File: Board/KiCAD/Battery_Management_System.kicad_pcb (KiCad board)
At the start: 4 copper layers, 104 parts, among them J1 Conn_01x06_Socket, J2 Conn_ARM_SWD_TagConnect_TC2030, J4 Conn_01x03, J5 Conn_01x03, J7 Conn_01x05, J8 Conn_01x02, J9 Conn_01x02, Q1 AON7408, Q10 AON7407, Q2 AON7408, Q23 2N7002, Q24 2N7002, Q25 2N7002, Q26 2N7002, Q3 AON7408, Q4 AON7408, Q5 BSS83P, Q6 BSS83P, Q7 BSS83P, Q8 BSS83P, SW2 SW_Push, U1 BQ25730RSNR, U3 LTC2943CDD_PBF, U4 INA260, U5 LMR50410, U6 INA260, U7 INA260, U8 INA260, U9 STM32F103C8T6, Y4 CM8V-T1A-32.768KHZ-12.5PF-20P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, Y5 8MHz

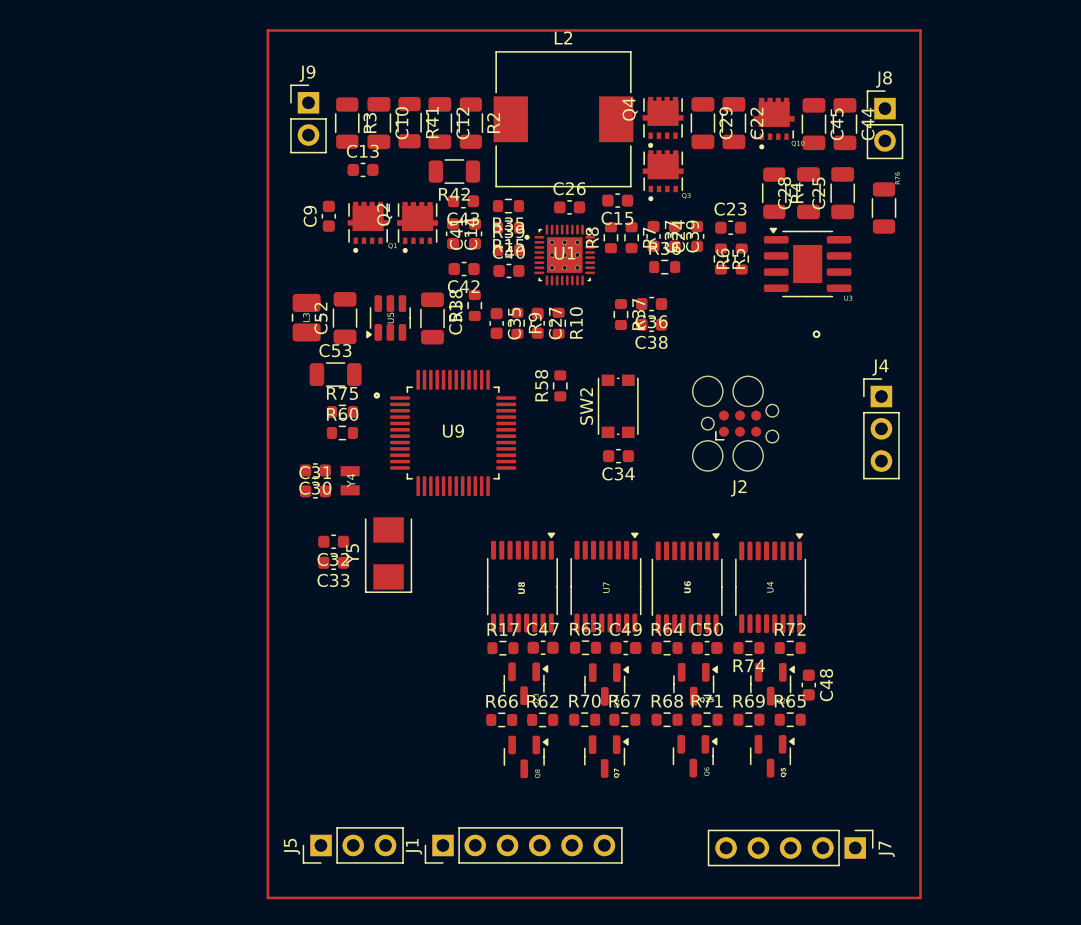
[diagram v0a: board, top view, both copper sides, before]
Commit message: Schematic: - Fixed FDI plug - Added thermistor connectors - Added a bunch of NCs using KiCAD NC tool - Added filter cap back into battery current shunt - Added bypass cap to LTC - Removed Cell 4 INA260 because the LTC does current, voltage of that top cell! Board Layout: - Chewed out team for not reading the BQ's datasheet, specifically Section 11 - Relayed out power stream using Section 11 as a refernce - Changed some footprints, mostly reducing size to 0603 - Positioned things optimally given what I thought made sense (dangerous, I know) - Fixed ground planes Other: - Removed PRL and CACHE files from the repo.
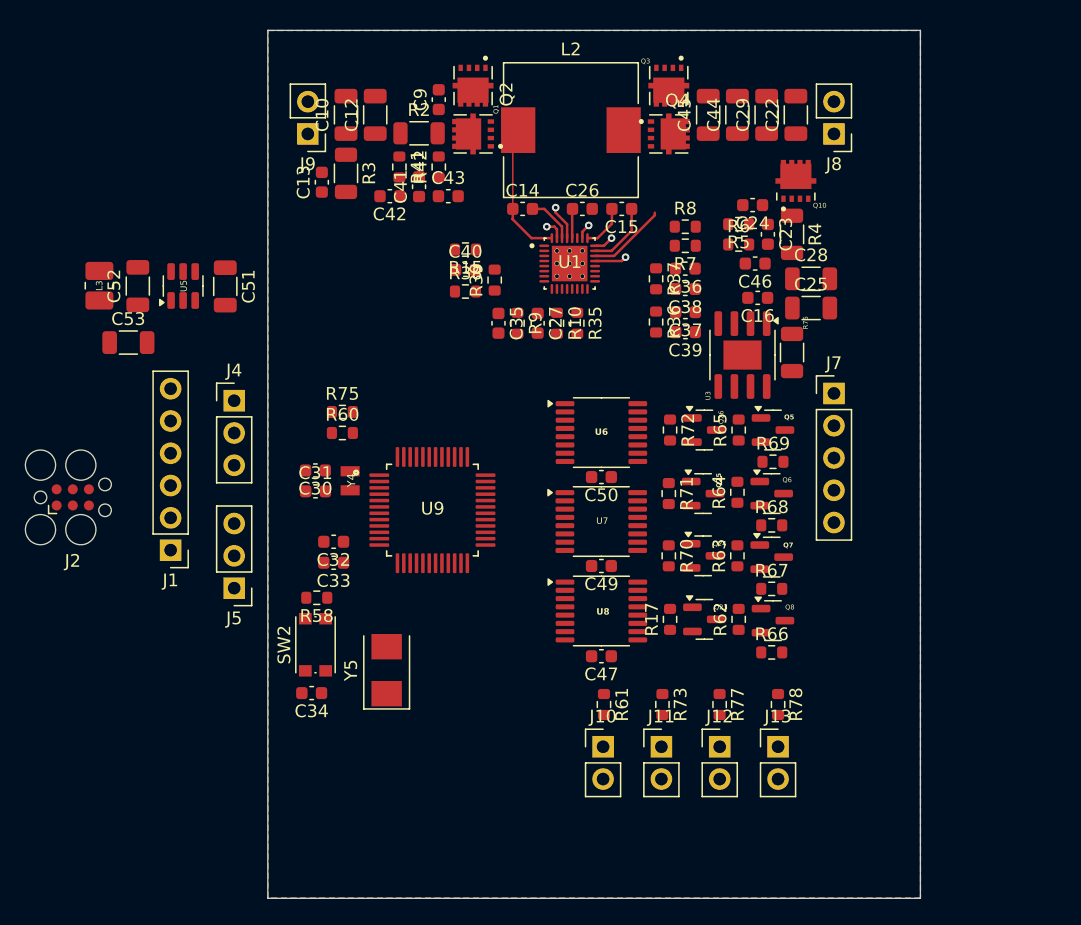
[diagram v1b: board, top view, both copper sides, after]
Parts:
- removed C48: 100n, Capacitor_SMD:C_0603_1608Metric
- removed R74: R_Small, Resistor_SMD:R_0603_1608Metric
- removed U4: INA260, Package_SO:TSSOP-16_4.4x5mm_P0.65mm
- added C16: 1uF, Capacitor_SMD:C_0603_1608Metric, F.Cu at (241.7, 67.7)
- added C46: 0.1uF, Capacitor_SMD:C_0603_1608Metric, F.Cu at (241.5, 65.0)
- added J10: Conn_01x02, Connector_PinHeader_2.54mm:PinHeader_1x02_P2.54mm_Vertical, F.Cu at (229.5, 103.0)
- added J11: Conn_01x02, Connector_PinHeader_2.54mm:PinHeader_1x02_P2.54mm_Vertical, F.Cu at (234.1, 103.0)
- added J12: Conn_01x02, Connector_PinHeader_2.54mm:PinHeader_1x02_P2.54mm_Vertical, F.Cu at (238.7, 103.0)
- added J13: Conn_01x02, Connector_PinHeader_2.54mm:PinHeader_1x02_P2.54mm_Vertical, F.Cu at (243.3, 103.0)
- added R61: 10k, Resistor_SMD:R_0603_1608Metric, F.Cu at (229.6, 99.7)
- added R73: 10k, Resistor_SMD:R_0603_1608Metric, F.Cu at (234.2, 99.7)
- added R77: 10k, Resistor_SMD:R_0603_1608Metric, F.Cu at (238.7, 99.7)
- added R78: 10k, Resistor_SMD:R_0603_1608Metric, F.Cu at (243.3, 99.7)
- R41, R42: footprint Resistor_SMD:R_1206_3216Metric -> Resistor_SMD:R_0603_1608Metric
- U3: value LTC2943CDD_PBF -> LTC2943CDD#PBF
- moved J2 52.8 mm to (187.8, 83.4)
- moved J4 50.9 mm to (200.5, 75.8)
- moved J7 35.8 mm to (247.7, 75.2), turned to 0 degrees
- moved J1 31.6 mm to (195.5, 87.5), turned to 180 degrees
- moved C34 30.5 mm to (206.6, 98.8)
- moved SW2 30.3 mm to (206.9, 95.0)
- moved Q5 25.7 mm to (242.9, 78.1), turned to 0 degrees
- moved R58 25.4 mm to (207.0, 91.3), turned to 180 degrees
- moved R65 23.2 mm to (240.2, 78.1), turned to 90 degrees
- moved Q8 22.3 mm to (242.9, 93.1), turned to 0 degrees
- moved R66 21.9 mm to (242.8, 95.6)
- moved Q6 21.6 mm to (242.8, 83.1), turned to 0 degrees
- moved J5 21.4 mm to (200.5, 90.5), turned to 180 degrees
- moved Q26 20.7 mm to (237.5, 78.1), turned to 0 degrees
- moved Q7 20.5 mm to (242.8, 88.1), turned to 0 degrees
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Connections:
- J1 pad 1: NC -> unconnected-(J1-Pin_1-Pad1)
- J1 pad 2: /Microcontroller/USART1_RX -> /Microcontroller/USART1_TX
- J1 pad 3: /Microcontroller/USART1_TX -> /Microcontroller/USART1_RX
- J1 pad 4: 3.3V -> unconnected-(J1-Pin_4-Pad4)
- J1 pad 5: NC -> unconnected-(J1-Pin_5-Pad5)
- J7 pad 1: /Cell Interface/Cell 4 -> /Cell Interface/BATT
- Q5 pad 3: /Cell Interface/Cell 4 -> /Cell Interface/BATT
- R65 pad 1: /Cell Interface/Cell 4 -> /Cell Interface/BATT
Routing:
- net Net-(U1-SW1): track 0.00 -> 10.9 mm
- net /Charge Control/Vsys: track 0.00 -> 6.23 mm
- net Net-(U1-SW2): track 0.00 -> 5.25 mm
- net Net-(U1-BTST1): track 0.00 -> 3.80 mm
- net Net-(U1-BTST2): track 0.00 -> 3.57 mm
- net Net-(U1-LODRV1): track 0.00 -> 2.77 mm, vias 0 -> 1
- net Net-(U1-~{BATDRV}): track 0.00 -> 2.52 mm, vias 0 -> 1
- net Net-(U1-REGN): track 0.00 -> 2.36 mm
- net Net-(U1-HIDRV1): track 0.00 -> 1.58 mm, vias 0 -> 1
- net Net-(U1-HIDRV2): track 0.00 -> 1.55 mm, vias 0 -> 1
- net Net-(U1-LODRV2): track 0.00 -> 1.21 mm, vias 0 -> 1
- net GND: vias 1 -> 0
- added copper zone on B.Cu, net GND
- added copper zone on F.Cu, net GND
- added copper zone on In2.Cu, net GND
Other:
- board outline added: 51.3 x 68.3 mm

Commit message: Schematic: - Changed to smaller 4 pin crystal - Added STM32 bypass caps Layout: - Added some example zones around vbus - Initial component placement for STM32 - Did an example Kelvin connection for shunt resistors - Added 3.3V power zone on layer 3 (PWR)
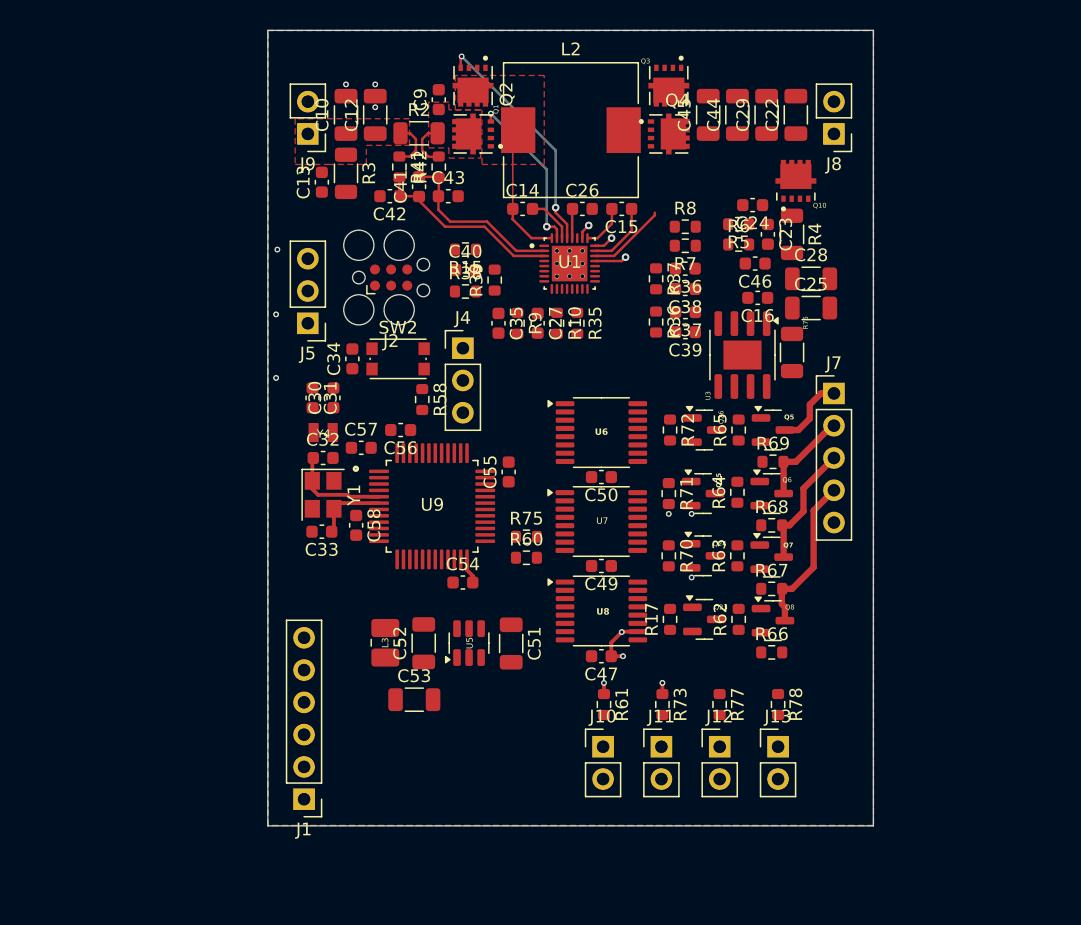
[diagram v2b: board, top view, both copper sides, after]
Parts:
- removed Y5: 8MHz, Crystal:Crystal_SMD_5032-2Pin_5.0x3.2mm
- added C54: 100n, Capacitor_SMD:C_0603_1608Metric, F.Cu at (218.5, 90.1)
- added C55: 100n, Capacitor_SMD:C_0603_1608Metric, F.Cu at (222.1, 81.4)
- added C56: 100n, Capacitor_SMD:C_0603_1608Metric, F.Cu at (213.6, 78.1)
- added C57: 100n, Capacitor_SMD:C_0603_1608Metric, F.Cu at (210.5, 79.5)
- added C58: 100n, Capacitor_SMD:C_0603_1608Metric, F.Cu at (210.1, 85.6)
- added Y1: Crystal_GND24_Small, Crystal:Crystal_SMD_TXC_7M-4Pin_3.2x2.5mm, F.Cu at (207.5, 83.2)
- moved C51 36.0 mm to (222.3, 94.9)
- moved C53 36.0 mm to (214.7, 99.3)
- moved C52 36.0 mm to (215.4, 94.9)
- moved L3 36.0 mm to (212.4, 94.8)
- moved U5 36.0 mm to (219.0, 94.9)
- moved J2 30.4 mm to (212.8, 66.1)
- moved C34 26.5 mm to (209.8, 72.5), turned to 90 degrees
- moved SW2 23.4 mm to (213.4, 72.5), turned to 0 degrees
- moved J1 22.2 mm to (206.0, 107.2)
- moved J5 21.6 mm to (206.3, 69.7)
- moved J4 18.5 mm to (218.5, 71.7)
- moved R58 17.7 mm to (215.3, 75.7), turned to -90 degrees
- moved R75 17.5 mm to (223.5, 86.5)
- moved R60 17.5 mm to (223.5, 88.2)
- moved C31 7.35 mm to (206.7, 75.6), turned to -90 degrees
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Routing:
- net Net-(U1-LODRV1): track 2.77 -> 18.7 mm, vias 1 -> 2
- net Net-(U1-ACP): track 0.00 -> 15.0 mm
- net Net-(U1-ACN): track 0.00 -> 13.8 mm
- net /Cell Interface/Cell 1: track 0.00 -> 12.5 mm
- net Net-(U1-HIDRV1): track 1.58 -> 12.9 mm, vias 1 -> 2
- net /Cell Interface/Cell 2: track 0.00 -> 9.87 mm
- net 3.3V: track 0.00 -> 8.24 mm, vias 0 -> 4
- net Net-(U9-PD0_OSC_IN): track 0.00 -> 7.97 mm
- net /Cell Interface/Cell 3: track 0.00 -> 7.66 mm
- net /Cell Interface/BATT: track 0.00 -> 5.70 mm
- net Net-(U9-PD1_OSC_OUT): track 0.00 -> 5.60 mm
- net Net-(C9-Pad1): track 0.00 -> 3.82 mm
- net /Charge Control/VBus: track 0.00 -> 3.80 mm
- net GND: vias 0 -> 9
- added copper zone on F.Cu, net /Charge Control/VBus
- added copper zone on In2.Cu, net 3.3V
- added copper zone on F.Cu, net Net-(C9-Pad1)
- added copper zone on F.Cu, net Net-(U1-SW1)
- removed copper zone on In2.Cu, net /Charge Control/VBus
- removed copper zone on In2.Cu, net /Charge Control/Vsys
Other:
- board size 51.3 x 68.3 mm -> 47.7 x 62.6 mm

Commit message: Added example test point
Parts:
- added TP1: TestPoint_Small, TestPoint:TestPoint_THTPad_1.0x1.0mm_Drill0.5mm, F.Cu at (205.4, 58.7)
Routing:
- net /Charge Control/VBus: track 3.80 -> 8.07 mm
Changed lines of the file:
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@@
 		)
 	)
+	(footprint "TestPoint:TestPoint_THTPad_1.0x1.0mm_Drill0.5mm"
+		(layer "F.Cu")
+		(at 205.4 58.7)
+		(descr "THT rectangular pad as test Point, square 1.0mm side length, hole diameter 0.5mm")
+		(tags "test point THT pad rectangle square")
+		(property "Reference" "TP1"
+			(at 0 -1.448 0)
+			(layer "F.SilkS")
+			(effects
+				(font
+					(size 1 1)
+					(thickness 0.15)
+				)
+			)
+		)
+		(property "Value" "TestPoint_Small"
+			(at 0 1.55 0)
+			(layer "F.Fab")
+			(effects
+				(font
+					(size 1 1)
+					(thickness 0.15)
+				)
+			)
+		)
+		(property "Datasheet" ""
+			(at 0 0 0)
+			(unlocked yes)
+			(layer "F.Fab")
+			(hide yes)
+			(effects
+				(font
+					(size 1.27 1.27)
+					(thickness 0.15)
+				)
+			)
+		)
+		(property "Description" "test point"
+			(at 0 0 0)
+			(unlocked yes)
+			(layer "F.Fab")
+			(hide yes)
+			(effects
+				(font
+					(size 1.27 1.27)
+					(thickness 0.15)
+				)
+			)
+		)
+		(property ki_fp_filters "Pin* Test*")
+		(sheetname "/")
+		(sheetfile "Battery_Management_System.kicad_sch")
+		(attr exclude_from_pos_files exclude_from_bom)
+		(fp_line
+			(start -0.7 -0.7)
+			(end 0.7 -0.7)
+			(stroke
+				(width 0.12)
+				(type solid)
+			)
+			(layer "F.SilkS")
+		)
+		(fp_line
+			(start -0.7 0.7)
+			(end -0.7 -0.7)
+			(stroke
+				(width 0.12)
+				(type solid)
+			)
+			(layer "F.SilkS")
+		)
+		(fp_line
+			(start 0.7 -0.7)
+			(end 0.7 0.7)
+			(stroke
+				(width 0.12)
+				(type solid)
+			)
+			(layer "F.SilkS")
+		)
+		(fp_line
+			(start 0.7 0.7)
+			(end -0.7 0.7)
+			(stroke
+				(width 0.12)
+				(type solid)
+			)
+			(layer "F.SilkS")
+		)
+		(fp_line
+			(start -1 -1)
+			(end -1 1)
+			(stroke
+				(width 0.05)
+				(type solid)
+			)
+			(layer "F.CrtYd")
+		)
+		(fp_line
+			(start -1 -1)
+			(end 1 -1)
+			(stroke
+				(width 0.05)
+				(type solid)
+			)
+			(layer "F.CrtYd")
+		)
+		(fp_line
+			(start 1 1)
+			(end -1 1)
+			(stroke
+				(width 0.05)
+				(type solid)
+			)
+			(layer "F.CrtYd")
+		)
+		(fp_line
+			(start 1 1)
+			(end 1 -1)
+			(stroke
+				(width 0.05)
+				(type solid)
+			)
+			(layer "F.CrtYd")
+		)
+		(fp_text user "${REFERENCE}"
+			(at 0 -1.45 0)
+			(layer "F.Fab")
+			(effects
+				(font
+					(size 1 1)
+					(thickness 0.15)
+				)
+			)
+		)
+		(pad "1" thru_hole rect
+			(at 0 0)
+			(size 1 1)
+			(drill 0.5)
+			(layers "*.Cu" "*.Mask")
+			(remove_unused_layers no)
+			(net 2 "/Charge Control/VBus")
+			(pinfunction "1")
+			(pintype "passive")
+		)
+		(embedded_fonts no)
+	)
 	(footprint "Resistor_SMD:R_1206_3216Metric"
 		(layer "F.Cu")
@@
 	)
 	(segment
+		(start 206.3 56.6)
+		(end 206.3 54.8)
+		(width 0.127)
+		(layer "F.Cu")
+		(net 2)
+	)
+	(segment
 		(start 213.5875 54.75)
 		(end 214.35 54.75)
@@
 	)
 	(segment
+		(start 205.4 57.5)
+		(end 206.3 56.6)
+		(width 0.127)
+		(layer "F.Cu")
+		(net 2)
+	)
+	(segment
 		(start 214.8 56.1)
 		(end 214.325 56.575)
@@
 	)
 	(segment
+		(start 205.4 58.7)
+		(end 205.4 57.5)
+		(width 0.127)
+		(layer "F.Cu")
+		(net 2)
+	)
+	(segment
 		(start 214.325 56.575)
 		(end 213.5 56.575)
@@
 		(polygon
 			(pts
-				(xy 205.3 57.2) (xy 207.9 57.2) (xy 207.9 57.2) (xy 210.9 57.2) (xy 210.9 55.7) (xy 214.3 55.7)
-				(xy 214.3 53.6) (xy 205.3 53.6)
+				(xy 205.3 57.2) (xy 207.9 57.2) (xy 210.9 57.2) (xy 210.9 55.7) (xy 214.3 55.7) (xy 214.3 53.6)
+				(xy 205.3 53.6)
 			)
 		)

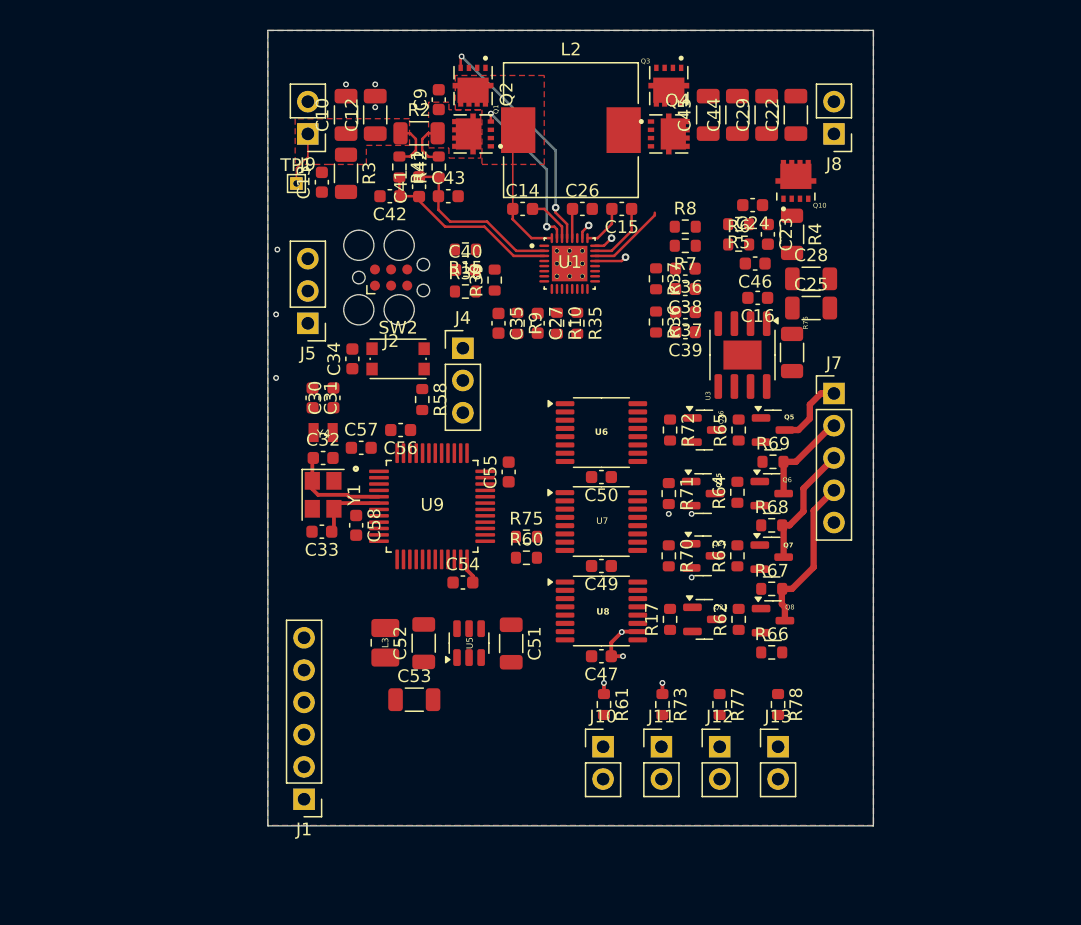
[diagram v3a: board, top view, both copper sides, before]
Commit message: New traces created
Populated lower half of PCB with new traces. Left most of the high voltage traces unchanged. Need Eyes on this ASAP
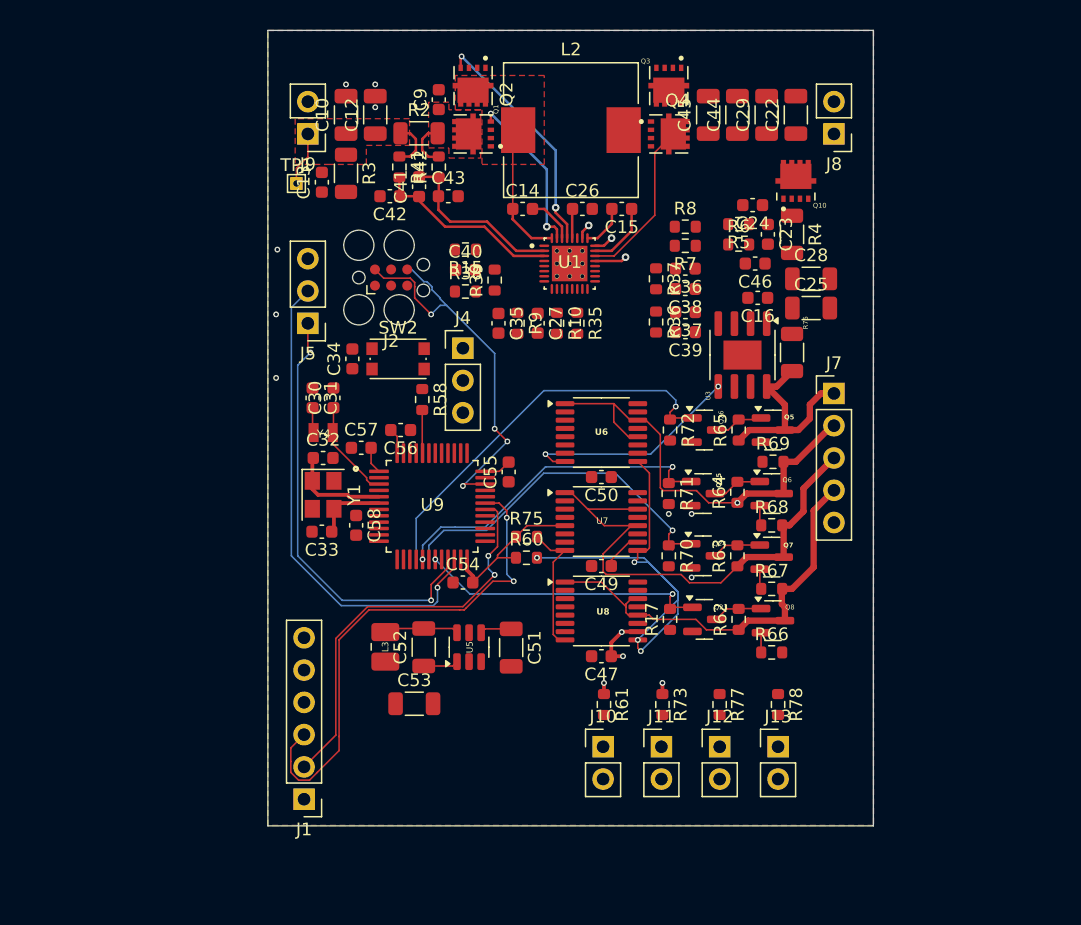
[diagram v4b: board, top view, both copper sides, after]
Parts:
- moved C51 0.32 mm to (222.3, 95.2)
- moved C52 0.32 mm to (215.4, 95.2)
- moved C53 0.32 mm to (214.7, 99.6)
- moved L3 0.32 mm to (212.4, 95.2)
- moved U5 0.32 mm to (219.0, 95.2)
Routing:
- net /Microcontroller/USART1_RX: track 0.00 -> 40.5 mm, vias 0 -> 2
- net /Microcontroller/I2C2_SDA_To_Host: track 0.00 -> 38.5 mm, vias 0 -> 1
- net /Cell Interface/SCL: track 0.00 -> 37.8 mm, vias 0 -> 4
- net /Microcontroller/I2C2_SCL_To_Host: track 0.00 -> 34.5 mm, vias 0 -> 2
- net /Microcontroller/USART1_TX: track 0.00 -> 32.2 mm, vias 0 -> 2
- net SWDIO: track 0.00 -> 32.0 mm, vias 0 -> 4
- net /Cell Interface/Cell_Balancer_4: track 0.00 -> 31.7 mm, vias 0 -> 1
- net /Cell Interface/Cell 2: track 9.87 -> 41.0 mm
- net /Cell Interface/SDA: track 0.00 -> 28.3 mm, vias 0 -> 2
- net /Cell Interface/Cell_Balancer_2: track 0.00 -> 27.6 mm, vias 0 -> 1
- net /Cell Interface/Cell 3: track 7.66 -> 34.7 mm, vias 0 -> 1
- net /Cell Interface/Cell_Balancer_3: track 0.00 -> 26.6 mm, vias 0 -> 2
- net /Cell Interface/Cell_Balancer_1: track 0.00 -> 22.9 mm, vias 0 -> 2
- net /Cell Interface/Cell 1: track 12.5 -> 33.3 mm
- net 3.3V: track 8.24 -> 28.3 mm
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
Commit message: Finished Traces
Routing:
- net 3.3V: track 28.3 -> 171.3 mm, vias 4 -> 15
- net GND: track 0.00 -> 78.9 mm, vias 9 -> 17
- net /Charge Control/VBus: track 10.6 -> 80.8 mm, vias 0 -> 2
- net /Cell Interface/SCL: track 37.8 -> 90.0 mm, vias 4 -> 8
- net /Microcontroller/Thermistor C3: track 0.00 -> 47.5 mm, vias 0 -> 1
- net VDDA: track 0.00 -> 45.1 mm, vias 0 -> 2
- net /Microcontroller/Thermistor C2: track 0.00 -> 43.7 mm, vias 0 -> 1
- net /Microcontroller/Thermistor C1: track 0.00 -> 41.4 mm, vias 0 -> 1
- net /Microcontroller/Thermistor C4: track 0.00 -> 41.3 mm, vias 0 -> 1
- net /Cell Interface/SDA: track 28.3 -> 62.9 mm, vias 2 -> 7
- net Net-(J2-~{RESET}): track 0.00 -> 27.8 mm, vias 0 -> 1
- net SWCLK: track 0.00 -> 25.2 mm, vias 0 -> 2
- net Net-(U1-~{BATDRV}): track 2.52 -> 21.1 mm, vias 1 -> 2
- net Net-(U1-SW2): track 5.25 -> 23.6 mm
- net Net-(U1-LODRV2): track 1.21 -> 17.5 mm, vias 1 -> 2
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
